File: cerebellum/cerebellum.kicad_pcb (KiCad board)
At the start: 2 copper layers, 91.5 x 52 mm, 82 parts, among them J1 PowerIn, J2 UART, J3 SWD_DBG, J4 SWD_DBG_PIN, J5 CAN FD, J6 CAN, Q1 AP2300, U1 OK1061-S, U2 TPS5430DDA, U3 BMI088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

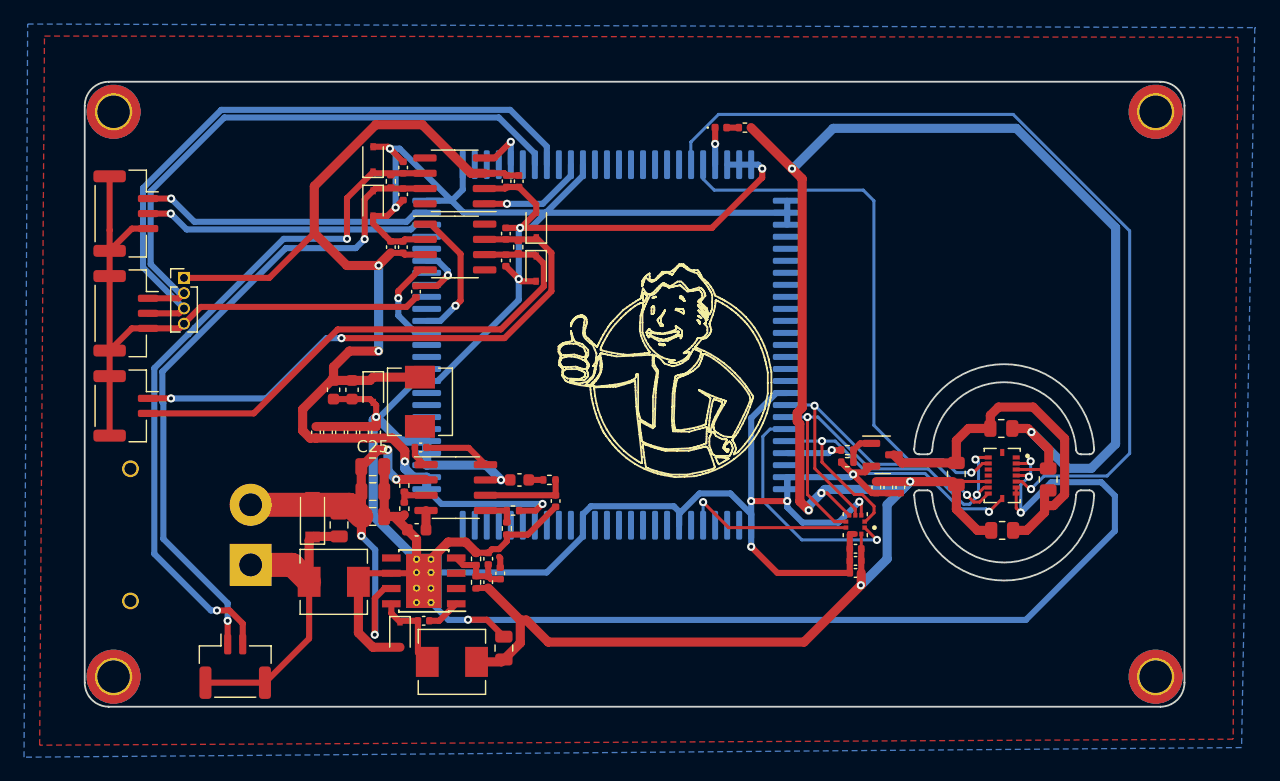
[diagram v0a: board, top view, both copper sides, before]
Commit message: [Modify] Change CAN ports sequence
2pin: 1-CAN_L, 2-CAN_H
3pin: 1-5V, 2-CAN_L, 3-CAN_H
4pin: 1,2-CAN_L, 3,4-CAN_H

Signed-off-by: Homalozoa <nx.tardis@gmail.com>
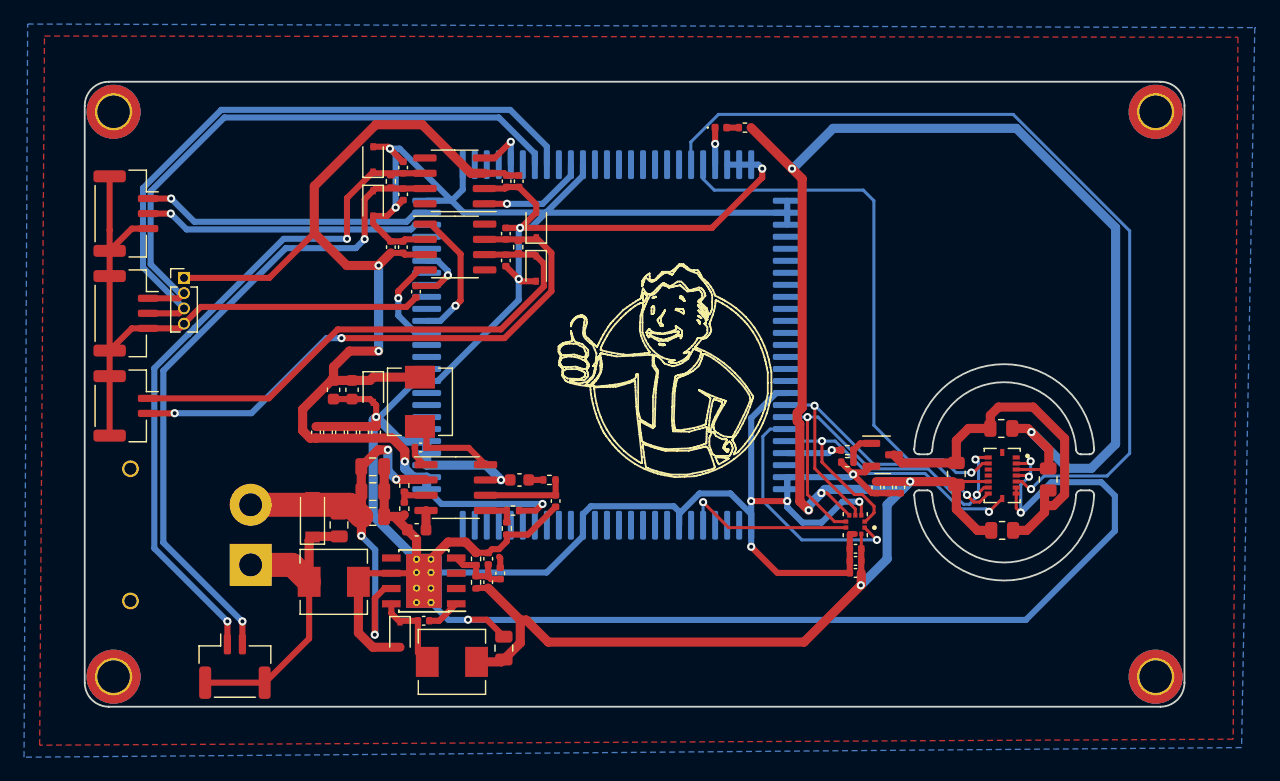
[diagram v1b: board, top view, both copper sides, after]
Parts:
- C33, C36: value 47uf/50V/0603 -> 47uf/6.3V/0603
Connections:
- J5 pad 1: CANFD_H -> CANFD_L
- J5 pad 2: CANFD_L -> CANFD_H
- J6 pad 1: CAN_H -> CAN_L
- J6 pad 2: CAN_L -> CAN_H
- Mount1 pad 1: (no net) -> GNDA
- Mount2 pad 1: (no net) -> GNDA
- Mount3 pad 1: (no net) -> GNDA
- Mount4 pad 1: (no net) -> GNDA
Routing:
- net Net-(C27-Pad1): track 5.51 -> 7.48 mm
- net CANFD_L: track 58.2 -> 56.8 mm
- net CAN_L: track 44.4 -> 43.9 mm
- net CAN_H: track 46.6 -> 47.1 mm

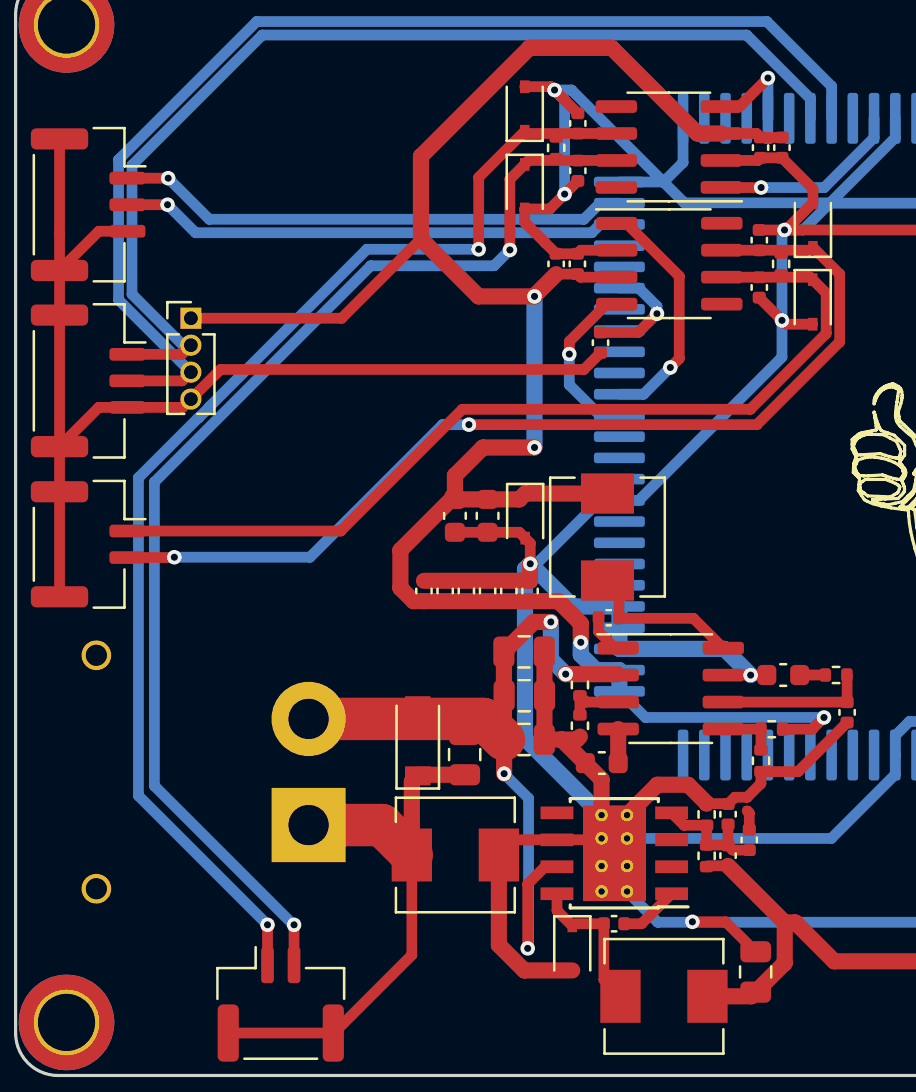
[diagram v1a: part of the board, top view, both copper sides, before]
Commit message: [Fix] Manufacture modification
Signed-off-by: Homalozoa <nx.tardis@gmail.com>
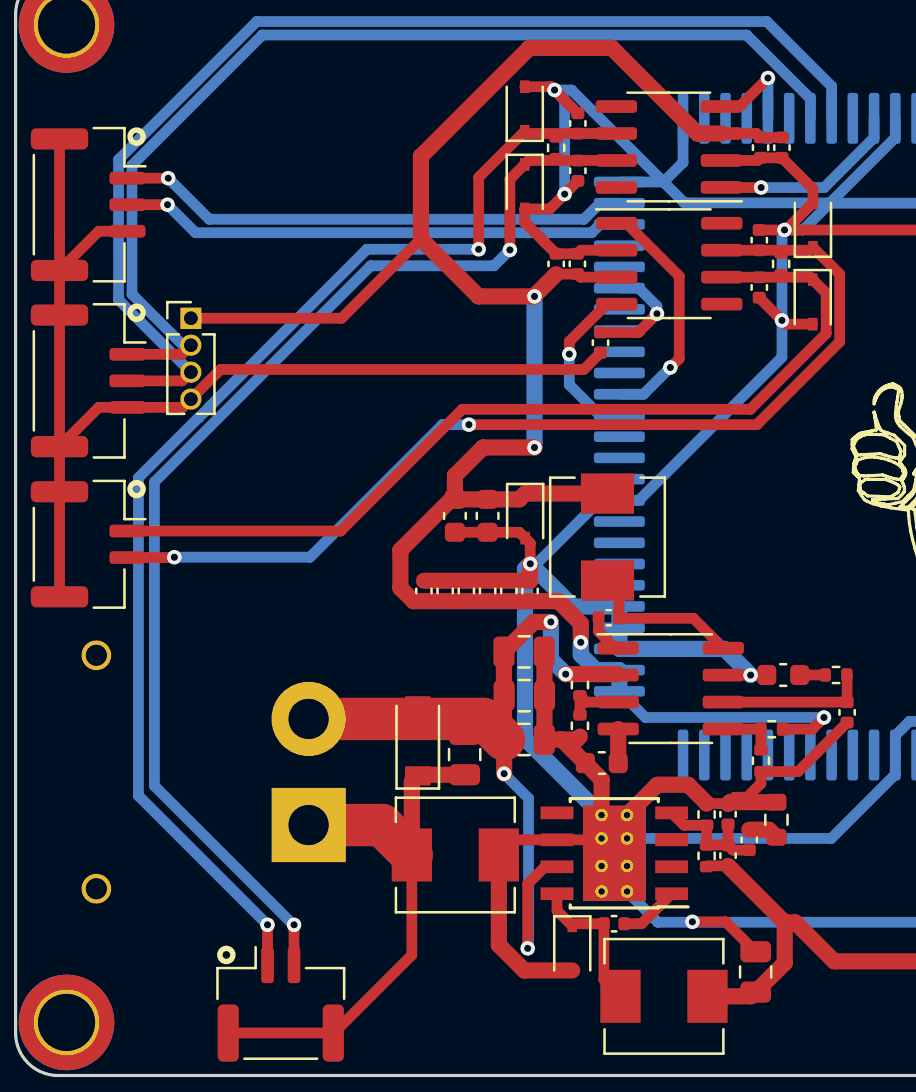
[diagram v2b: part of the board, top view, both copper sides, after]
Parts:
- C19: value 100uf/50V/0805 -> 100uf/6.3V/0805
- D3, D4, D6, D7: value 12V -> BV12C
- R11: value 549R/0201 -> 549R/0603; footprint Resistor_SMD:R_0201_0603Metric -> Resistor_SMD:R_0603_1608Metric
- moved R11 1.57 mm to (140.1, 114.0)
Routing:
- net GND: track 432.7 -> 435.0 mm
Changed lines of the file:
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@@
       (svguseinch false)
       (svgprecision 6)
-      (excludeedgelayer true)
+      (excludeedgelayer false)
       (plotframeref false)
       (viasonmask false)
@@
       (effects (font (size 0.8 1) (thickness 0.15)))
     )
-    (fp_text value "12V" (at 0.1 1.9 90) (layer "F.Fab") hide
+    (fp_text value "BV12C" (at 0.1 1.9 90) (layer "F.Fab") hide
       (effects (font (size 1 1) (thickness 0.15)))
     )
@@
       (effects (font (size 1 1) (thickness 0.15)))
     )
-    (fp_text value "12V" (at 0.1 1.9 -270) (layer "F.Fab") hide
+    (fp_text value "BV12C" (at 0.1 1.9 -270) (layer "F.Fab") hide
       (effects (font (size 1 1) (thickness 0.15)))
     )
@@
     )
   )
-  (footprint "Resistor_SMD:R_0201_0603Metric" (layer "F.Cu")
-    (at 138.72 113.21 90)
-    (descr "Resistor SMD 0201 (0603 Metric), square (rectangular) end terminal, IPC_7351 nominal, (Body size source: https://www.vishay.com/docs/20052/crcw0201e3.pdf), generated with kicad-footprint-generator")
+  (footprint "Resistor_SMD:R_0603_1608Metric" (layer "F.Cu")
+    (at 140.1 113.95 90)
+    (descr "Resistor SMD 0603 (1608 Metric), square (rectangular) end terminal, IPC_7351 nominal, (Body size source: IPC-SM-782 page 72, https://www.pcb-3d.com/wordpress/wp-content/uploads/ipc-sm-782a_amendment_1_and_2.pdf), generated with kicad-footprint-generator")
     (tags "resistor")
     (property "Sheetfile" "cerebellum.kicad_sch")
     (property "Sheetname" "")
     (attr smd)
-    (fp_text reference "R11" (at -0.6 -1.07 90) (layer "F.SilkS") hide
-      (effects (font (size 0.8 1) (thickness 0.15)))
+    (fp_text reference "R11" (at 0 -1.43 90) (layer "F.SilkS") hide
+      (effects (font (size 1 1) (thickness 0.15)))
     )
-    (fp_text value "549R/0201" (at 0 1.05 90) (layer "F.Fab") hide
+    (fp_text value "549R/0603" (at 0 1.43 90) (layer "F.Fab") hide
       (effects (font (size 1 1) (thickness 0.15)))
     )
-    (fp_text user "${REFERENCE}" (at 0 -0.68 90) (layer "F.Fab") hide
-      (effects (font (size 0.25 0.25) (thickness 0.04)))
+    (fp_text user "${REFERENCE}" (at 0 0 90) (layer "F.Fab") hide
+      (effects (font (size 0.4 0.4) (thickness 0.06)))
     )
-    (fp_line (start 0.7 0.35) (end -0.7 0.35) (layer "F.CrtYd") (width 0.05))
-    (fp_line (start -0.7 -0.35) (end 0.7 -0.35) (layer "F.CrtYd") (width 0.05))
-    (fp_line (start 0.7 -0.35) (end 0.7 0.35) (layer "F.CrtYd") (width 0.05))
-    (fp_line (start -0.7 0.35) (end -0.7 -0.35) (layer "F.CrtYd") (width 0.05))
-    (fp_line (start -0.3 -0.15) (end 0.3 -0.15) (layer "F.Fab") (width 0.1))
-    (fp_line (start 0.3 0.15) (end -0.3 0.15) (layer "F.Fab") (width 0.1))
-    (fp_line (start -0.3 0.15) (end -0.3 -0.15) (layer "F.Fab") (width 0.1))
-    (fp_line (start 0.3 -0.15) (end 0.3 0.15) (layer "F.Fab") (width 0.1))
-    (pad "" smd roundrect (at -0.345 0 90) (size 0.318 0.36) (layers "F.Paste") (roundrect_rratio 0.25))
-    (pad "" smd roundrect (at 0.345 0 90) (size 0.318 0.36) (layers "F.Paste") (roundrect_rratio 0.25))
-    (pad "1" smd roundrect (at -0.32 0 90) (size 0.46 0.4) (layers "F.Cu" "F.Mask") (roundrect_rratio 0.25)
+    (fp_line (start -0.237258 -0.5225) (end 0.237258 -0.5225) (layer "F.SilkS") (width 0.12))
+    (fp_line (start -0.237258 0.5225) (end 0.237258 0.5225) (layer "F.SilkS") (width 0.12))
+    (fp_line (start -1.48 -0.73) (end 1.48 -0.73) (layer "F.CrtYd") (width 0.05))
+    (fp_line (start -1.48 0.73) (end -1.48 -0.73) (layer "F.CrtYd") (width 0.05))
+    (fp_line (start 1.48 -0.73) (end 1.48 0.73) (layer "F.CrtYd") (width 0.05))
+    (fp_line (start 1.48 0.73) (end -1.48 0.73) (layer "F.CrtYd") (width 0.05))
+    (fp_line (start 0.8 0.4125) (end -0.8 0.4125) (layer "F.Fab") (width 0.1))
+    (fp_line (start -0.8 0.4125) (end -0.8 -0.4125) (layer "F.Fab") (width 0.1))
+    (fp_line (start 0.8 -0.4125) (end 0.8 0.4125) (layer "F.Fab") (width 0.1))
+    (fp_line (start -0.8 -0.4125) (end 0.8 -0.4125) (layer "F.Fab") (width 0.1))
+    (pad "1" smd roundrect (at -0.825 0 90) (size 0.8 0.95) (layers "F.Cu" "F.Paste" "F.Mask") (roundrect_rratio 0.25)
       (net 9 "Net-(C24-Pad2)") (pintype "passive"))
-    (pad "2" smd roundrect (at 0.32 0 90) (size 0.46 0.4) (layers "F.Cu" "F.Mask") (roundrect_rratio 0.25)
+    (pad "2" smd roundrect (at 0.825 0 90) (size 0.8 0.95) (layers "F.Cu" "F.Paste" "F.Mask") (roundrect_rratio 0.25)
       (net 1 "GND") (pintype "passive"))
-    (model "${KICAD6_3DMODEL_DIR}/Resistor_SMD.3dshapes/R_0201_0603Metric.wrl"
+    (model "${KICAD6_3DMODEL_DIR}/Resistor_SMD.3dshapes/R_0603_1608Metric.wrl"
       (offset (xyz 0 0 0))
       (scale (xyz 1 1 1))
@@
       (effects (font (size 0.8 1) (thickness 0.15)))
     )
-    (fp_text value "100uf/50V/0805" (at 0 1.68 90) (layer "F.Fab") hide
+    (fp_text value "100uf/6.3V/0805" (at 0 1.68 90) (layer "F.Fab") hide
       (effects (font (size 1 1) (thickness 0.15)))
     )
@@
       (effects (font (size 0.8 1) (thickness 0.15)))
     )
-    (fp_text value "12V" (at 0.1 1.9 90) (layer "F.Fab") hide
+    (fp_text value "BV12C" (at 0.1 1.9 90) (layer "F.Fab") hide
       (effects (font (size 1 1) (thickness 0.15)))
     )
@@
     (property "Sheetfile" "cerebellum.kicad_sch")
     (property "Sheetname" "")
-    (attr through_hole)
+    (attr through_hole exclude_from_pos_files)
     (fp_text reference "J3" (at -1.1 5.87 90) (layer "F.SilkS") hide
       (effects (font (size 0.8 1) (thickness 0.15)))
@@
       (effects (font (size 1 1) (thickness 0.15)))
     )
-    (fp_text value "12V" (at 0.1 1.9 90) (layer "F.Fab") hide
+    (fp_text value "BV12C" (at 0.1 1.9 90) (layer "F.Fab") hide
       (effects (font (size 1 1) (thickness 0.15)))
     )
@@
     (property "Sheetfile" "cerebellum.kicad_sch")
     (property "Sheetname" "")
-    (attr through_hole)
+    (attr through_hole exclude_from_pos_files)
     (fp_text reference "J1" (at -2.5 14.5 90) (layer "B.SilkS") hide
       (effects (font (size 1 1) (thickness 0.15)) (justify mirror))
@@
     (property "Sheetfile" "cerebellum.kicad_sch")
     (property "Sheetname" "")
-    (attr smd)
+    (attr smd exclude_from_pos_files)
     (fp_text reference "U1" (at 0.39 1.57 270 unlocked) (layer "B.SilkS") hide
       (effects (font (size 1 1) (thickness 0.15)) (justify mirror))
@@
   (gr_line (start 153.302247 100.981388) (end 153.340338 99.766388) (layer "F.SilkS") (width 0.15))
   (gr_line (start 144.742729 94.866614) (end 144.721692 94.799091) (layer "F.SilkS") (width 0.15))
+  (gr_circle (center 109.951 98.37) (end 110.26 98.37) (layer "F.SilkS") (width 0.254) (fill none))
   (gr_arc (start 150.704834 104.225334) (mid 150.70921 104.202135) (end 150.71613 104.179563) (layer "F.SilkS") (width 0.15))
   (gr_line (start 145.653645 95.834996) (end 145.346145 95.725766) (layer "F.SilkS") (width 0.15))
@@
   (gr_line (start 154.073085 89.183888) (end 153.890865 89.185133) (layer "F.SilkS") (width 0.15))
   (gr_line (start 152.257396 104.632597) (end 152.561147 104.709728) (layer "F.SilkS") (width 0.15))
+  (gr_circle (center 109.951 81.76) (end 110.26 81.76) (layer "F.SilkS") (width 0.254) (fill none))
   (gr_arc (start 146.001048 97.340479) (mid 146.012343 97.353931) (end 146.021877 97.368684) (layer "F.SilkS") (width 0.15))
   (gr_arc (start 151.146196 96.334879) (mid 151.020788 96.157468) (end 150.90713 95.97231) (layer "F.SilkS") (width 0.15))
@@
   (gr_line (start 147.021615 96.850813) (end 147.040252 96.881375) (layer "F.SilkS") (width 0.15))
   (gr_arc (start 159.168199 104.620896) (mid 158.732585 105.031983) (end 158.265718 105.407199) (layer "F.SilkS") (width 0.15))
+  (gr_circle (center 114.181 120.32) (end 114.49 120.32) (layer "F.SilkS") (width 0.254) (fill none))
   (gr_line (start 144.157673 98.008177) (end 144.288645 97.914966) (layer "F.SilkS") (width 0.15))
   (gr_line (start 144.767656 94.951388) (end 144.742729 94.866614) (layer "F.SilkS") (width 0.15))
@@
   (gr_line (start 154.779781 91.401896) (end 154.916145 91.380932) (layer "F.SilkS") (width 0.15))
   (gr_arc (start 153.569523 93.027347) (mid 153.609941 93.040024) (end 153.649335 93.055596) (layer "F.SilkS") (width 0.15))
+  (gr_circle (center 109.951 90.06) (end 110.26 90.06) (layer "F.SilkS") (width 0.254) (fill none))
   (gr_line (start 150.048898 98.957702) (end 150.058531 99.164735) (layer "F.SilkS") (width 0.15))
   (gr_line (start 154.649145 91.420939) (end 154.779781 91.401896) (layer "F.SilkS") (width 0.15))
@@
   (segment (start 182.7125 106.7625) (end 182.81 106.86) (width 0.254) (layer "F.Cu") (net 1))
   (segment (start 139.37 112.24) (end 138.72 112.89) (width 0.508) (layer "F.Cu") (net 1))
+  (segment (start 137.905 113.125) (end 137.82 113.21) (width 0.762) (layer "F.Cu") (net 1))
+  (segment (start 140.1 113.125) (end 137.905 113.125) (width 0.762) (layer "F.Cu") (net 1))
   (segment (start 130.84 110.03) (end 130.7 110.17) (width 0.762) (layer "F.Cu") (net 1))
   (segment (start 139.37 111.68) (end 139.37 112.24) (width 0.508) (layer "F.Cu") (net 1))
@@
   (segment (start 124.3666 95.3334) (end 125.61 95.3334) (width 0.508) (layer "B.Cu") (net 8))
   (segment (start 118.12 101.58) (end 124.3666 95.3334) (width 0.508) (layer "B.Cu") (net 8))
-  (segment (start 138.82 113.63) (end 138.72 113.53) (width 0.508) (layer "F.Cu") (net 9))
-  (segment (start 138.82 114.42) (end 138.82 113.63) (width 0.508) (layer "F.Cu") (net 9))
+  (segment (start 139.745 114.42) (end 140.1 114.775) (width 0.762) (layer "F.Cu") (net 9))
+  (segment (start 138.82 114.42) (end 139.745 114.42) (width 0.762) (layer "F.Cu") (net 9))
   (segment (start 112.08 92.02) (end 112.51 91.59) (width 0.508) (layer "F.Cu") (net 10))
   (segment (start 109.52 92.02) (end 112.08 92.02) (width 0.508) (layer "F.Cu") (net 10))
